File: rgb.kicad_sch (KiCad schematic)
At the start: 0 parts

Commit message: chore: add led matrix
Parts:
- added LED1, LED10, LED11, LED12, LED13, LED14, LED15, LED16, LED17, LED18, LED19, LED2, LED20, LED21, LED22, LED23, LED24, LED25, LED26, LED27, LED28, LED29, LED3, LED30, LED31, LED32, LED33, LED34, LED35, LED36, LED37, LED38, LED39, LED4, LED40, LED41, LED42, LED43, LED44, LED45, LED46, LED5, LED6, LED7, LED8, LED9: MX_SK6812MINI-E, PCM_marbastlib-mx:LED_MX_6028R, symbol PCM_marbastlib-mx:MX_SK6812MINI-E
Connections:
- new net: LED12.2 (DOUT), LED24.3 (DIN)
- new net: LED11.2 (DOUT), LED12.3 (DIN)
- new net: LED26.2 (DOUT), LED27.3 (DIN)
- new net: LED25.2 (DOUT), LED26.3 (DIN)
- new net: LED44.3 (DIN), LED45.2 (DOUT)
- new net: LED45.3 (DIN), LED46.2 (DOUT)
- new net: LED1.2 (DOUT), LED2.3 (DIN)
- new net: LED13.2 (DOUT), LED25.3 (DIN)
- new net: LED42.3 (DIN), LED43.2 (DOUT)
- new net: LED43.3 (DIN), LED44.2 (DOUT)
- new net: LED18.3 (DIN), LED19.2 (DOUT)
- new net: LED19.3 (DIN), LED20.2 (DOUT)
- new net: LED31.2 (DOUT), LED32.3 (DIN)
- new net: LED30.2 (DOUT), LED31.3 (DIN)
- new net: LED13.3 (DIN), LED14.2 (DOUT)
- new net: LED3.2 (DOUT), LED4.3 (DIN)
- new net: LED2.2 (DOUT), LED3.3 (DIN)
- new net: LED16.3 (DIN), LED17.2 (DOUT)
- new net: LED17.3 (DIN), LED18.2 (DOUT)
- new net: LED29.2 (DOUT), LED30.3 (DIN)
- new net: LED28.2 (DOUT), LED29.3 (DIN)
- new net: LED36.2 (DOUT), LED46.3 (DIN)
- new net: LED41.3 (DIN), LED42.2 (DOUT)
- new net: LED5.2 (DOUT), LED6.3 (DIN)
- new net: LED4.2 (DOUT), LED5.3 (DIN)
- new net: LED14.3 (DIN), LED15.2 (DOUT)
- new net: LED15.3 (DIN), LED16.2 (DOUT)
- new net: LED23.3 (DIN), LED24.2 (DOUT)
- new net: LED35.2 (DOUT), LED36.3 (DIN)
- new net: LED22.3 (DIN), LED23.2 (DOUT)
- new net: LED20.3 (DIN), LED21.2 (DOUT)
- new net: LED21.3 (DIN), LED22.2 (DOUT)
- new net: LED33.2 (DOUT), LED34.3 (DIN)
- new net: LED32.2 (DOUT), LED33.3 (DIN)
- new net: LED10.2 (DOUT), LED11.3 (DIN)
- new net: LED6.2 (DOUT), LED7.3 (DIN)
- new net: LED37.3 (DIN), LED38.2 (DOUT)
- new net: LED7.2 (DOUT), LED8.3 (DIN)
- new net: LED8.2 (DOUT), LED9.3 (DIN)
- new net: LED10.3 (DIN), LED9.2 (DOUT)
- new net: LED27.2 (DOUT), LED28.3 (DIN)
- new net: LED34.2 (DOUT), LED35.3 (DIN)
- new net: LED38.3 (DIN), LED39.2 (DOUT)
- new net: LED39.3 (DIN), LED40.2 (DOUT)
- new net: LED40.3 (DIN), LED41.2 (DOUT)
- new net +5V: LED1.1 (VDD), LED10.1 (VDD), LED11.1 (VDD), LED12.1 (VDD), LED13.1 (VDD), LED14.1 (VDD), LED15.1 (VDD), LED16.1 (VDD), LED17.1 (VDD), LED18.1 (VDD), LED19.1 (VDD), LED2.1 (VDD), LED20.1 (VDD), LED21.1 (VDD), LED22.1 (VDD), LED23.1 (VDD), LED24.1 (VDD), LED25.1 (VDD), LED26.1 (VDD), LED27.1 (VDD), LED28.1 (VDD), LED29.1 (VDD), LED3.1 (VDD), LED30.1 (VDD), LED31.1 (VDD), LED32.1 (VDD), LED33.1 (VDD), LED34.1 (VDD), LED35.1 (VDD), LED36.1 (VDD), LED37.1 (VDD), LED38.1 (VDD), LED39.1 (VDD), LED4.1 (VDD), LED40.1 (VDD), LED41.1 (VDD), LED42.1 (VDD), LED43.1 (VDD), LED44.1 (VDD), LED45.1 (VDD), LED46.1 (VDD), LED5.1 (VDD), LED6.1 (VDD), LED7.1 (VDD), LED8.1 (VDD), LED9.1 (VDD)
- new net GND: LED1.4 (VSS), LED10.4 (VSS), LED11.4 (VSS), LED12.4 (VSS), LED13.4 (VSS), LED14.4 (VSS), LED15.4 (VSS), LED16.4 (VSS), LED17.4 (VSS), LED18.4 (VSS), LED19.4 (VSS), LED2.4 (VSS), LED20.4 (VSS), LED21.4 (VSS), LED22.4 (VSS), LED23.4 (VSS), LED24.4 (VSS), LED25.4 (VSS), LED26.4 (VSS), LED27.4 (VSS), LED28.4 (VSS), LED29.4 (VSS), LED3.4 (VSS), LED30.4 (VSS), LED31.4 (VSS), LED32.4 (VSS), LED33.4 (VSS), LED34.4 (VSS), LED35.4 (VSS), LED36.4 (VSS), LED37.4 (VSS), LED38.4 (VSS), LED39.4 (VSS), LED4.4 (VSS), LED40.4 (VSS), LED41.4 (VSS), LED42.4 (VSS), LED43.4 (VSS), LED44.4 (VSS), LED45.4 (VSS), LED46.4 (VSS), LED5.4 (VSS), LED6.4 (VSS), LED7.4 (VSS), LED8.4 (VSS), LED9.4 (VSS)
- new net RGB 5V: LED1.3 (DIN)
- no-connect marks 0 -> 1

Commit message: chore: set up layout
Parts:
- LED1, LED10, LED11, LED12, LED2, LED25, LED26, LED27, LED28, LED29, LED3, LED30, LED31, LED32, LED33, LED34, LED35, LED36, LED4, LED5, LED6, LED7, LED8, LED9: footprint PCM_marbastlib-mx:LED_MX_6028R -> PCM_marbastlib-mx:LED_MX_6028R-ROT
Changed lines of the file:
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@@
 			)
 		)
-		(property "Footprint" "PCM_marbastlib-mx:LED_MX_6028R"
+		(property "Footprint" "PCM_marbastlib-mx:LED_MX_6028R-ROT"
 			(at 330.2 50.8 0)
 			(effects
@@
 			)
 		)
-		(property "Footprint" "PCM_marbastlib-mx:LED_MX_6028R"
+		(property "Footprint" "PCM_marbastlib-mx:LED_MX_6028R-ROT"
 			(at 76.2 127 0)
 			(effects
@@
 			)
 		)
-		(property "Footprint" "PCM_marbastlib-mx:LED_MX_6028R"
+		(property "Footprint" "PCM_marbastlib-mx:LED_MX_6028R-ROT"
 			(at 50.8 50.8 0)
 			(effects
@@
 			)
 		)
-		(property "Footprint" "PCM_marbastlib-mx:LED_MX_6028R"
+		(property "Footprint" "PCM_marbastlib-mx:LED_MX_6028R-ROT"
 			(at 50.8 127 0)
 			(effects
@@
 			)
 		)
-		(property "Footprint" "PCM_marbastlib-mx:LED_MX_6028R"
+		(property "Footprint" "PCM_marbastlib-mx:LED_MX_6028R-ROT"
 			(at 203.2 127 0)
 			(effects
@@
 			)
 		)
-		(property "Footprint" "PCM_marbastlib-mx:LED_MX_6028R"
+		(property "Footprint" "PCM_marbastlib-mx:LED_MX_6028R-ROT"
 			(at 101.6 50.8 0)
 			(effects
@@
 			)
 		)
-		(property "Footprint" "PCM_marbastlib-mx:LED_MX_6028R"
+		(property "Footprint" "PCM_marbastlib-mx:LED_MX_6028R-ROT"
 			(at 152.4 127 0)
 			(effects
@@
 			)
 		)
-		(property "Footprint" "PCM_marbastlib-mx:LED_MX_6028R"
+		(property "Footprint" "PCM_marbastlib-mx:LED_MX_6028R-ROT"
 			(at 152.4 50.8 0)
 			(effects
@@
 			)
 		)
-		(property "Footprint" "PCM_marbastlib-mx:LED_MX_6028R"
+		(property "Footprint" "PCM_marbastlib-mx:LED_MX_6028R-ROT"
 			(at 330.2 127 0)
 			(effects
@@
 			)
 		)
-		(property "Footprint" "PCM_marbastlib-mx:LED_MX_6028R"
+		(property "Footprint" "PCM_marbastlib-mx:LED_MX_6028R-ROT"
 			(at 127 50.8 0)
 			(effects
@@
 			)
 		)
-		(property "Footprint" "PCM_marbastlib-mx:LED_MX_6028R"
+		(property "Footprint" "PCM_marbastlib-mx:LED_MX_6028R-ROT"
 			(at 254 127 0)
 			(effects
@@
 			)
 		)
-		(property "Footprint" "PCM_marbastlib-mx:LED_MX_6028R"
+		(property "Footprint" "PCM_marbastlib-mx:LED_MX_6028R-ROT"
 			(at 304.8 50.8 0)
 			(effects
@@
 			)
 		)
-		(property "Footprint" "PCM_marbastlib-mx:LED_MX_6028R"
+		(property "Footprint" "PCM_marbastlib-mx:LED_MX_6028R-ROT"
 			(at 177.8 50.8 0)
 			(effects
@@
 			)
 		)
-		(property "Footprint" "PCM_marbastlib-mx:LED_MX_6028R"
+		(property "Footprint" "PCM_marbastlib-mx:LED_MX_6028R-ROT"
 			(at 203.2 50.8 0)
 			(effects
@@
 			)
 		)
-		(property "Footprint" "PCM_marbastlib-mx:LED_MX_6028R"
+		(property "Footprint" "PCM_marbastlib-mx:LED_MX_6028R-ROT"
 			(at 228.6 50.8 0)
 			(effects
@@
 			)
 		)
-		(property "Footprint" "PCM_marbastlib-mx:LED_MX_6028R"
+		(property "Footprint" "PCM_marbastlib-mx:LED_MX_6028R-ROT"
 			(at 279.4 50.8 0)
 			(effects
@@
 			)
 		)
-		(property "Footprint" "PCM_marbastlib-mx:LED_MX_6028R"
+		(property "Footprint" "PCM_marbastlib-mx:LED_MX_6028R-ROT"
 			(at 76.2 50.8 0)
 			(effects
@@
 			)
 		)
-		(property "Footprint" "PCM_marbastlib-mx:LED_MX_6028R"
+		(property "Footprint" "PCM_marbastlib-mx:LED_MX_6028R-ROT"
 			(at 127 127 0)
 			(effects
@@
 			)
 		)
-		(property "Footprint" "PCM_marbastlib-mx:LED_MX_6028R"
+		(property "Footprint" "PCM_marbastlib-mx:LED_MX_6028R-ROT"
 			(at 279.4 127 0)
 			(effects
@@
 			)
 		)
-		(property "Footprint" "PCM_marbastlib-mx:LED_MX_6028R"
+		(property "Footprint" "PCM_marbastlib-mx:LED_MX_6028R-ROT"
 			(at 254 50.8 0)
 			(effects
@@
 			)
 		)
-		(property "Footprint" "PCM_marbastlib-mx:LED_MX_6028R"
+		(property "Footprint" "PCM_marbastlib-mx:LED_MX_6028R-ROT"
 			(at 101.6 127 0)
 			(effects
@@
 			)
 		)
-		(property "Footprint" "PCM_marbastlib-mx:LED_MX_6028R"
+		(property "Footprint" "PCM_marbastlib-mx:LED_MX_6028R-ROT"
 			(at 304.8 127 0)
 			(effects
@@
 			)
 		)
-		(property "Footprint" "PCM_marbastlib-mx:LED_MX_6028R"
+		(property "Footprint" "PCM_marbastlib-mx:LED_MX_6028R-ROT"
 			(at 177.8 127 0)
 			(effects
@@
 			)
 		)
-		(property "Footprint" "PCM_marbastlib-mx:LED_MX_6028R"
+		(property "Footprint" "PCM_marbastlib-mx:LED_MX_6028R-ROT"
 			(at 228.6 127 0)
 			(effects

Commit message: chore: open-drain for rgb
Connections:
- net RGB 5V renamed RGB5V
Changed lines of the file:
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@@
 		)
 	)
-	(global_label "RGB 5V"
+	(global_label "RGB5V"
 		(shape input)
 		(at 43.18 50.8 180)
@@
 		)
 		(property "Intersheetrefs" "${INTERSHEET_REFS}"
-			(at 33.1191 50.8 0)
+			(at 34.0867 50.8 0)
 			(effects
 				(font

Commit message: chore: add mounting holes
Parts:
- LED1: LCSC (none) -> C5149201
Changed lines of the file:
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@@
+			)
+		)
+		(property "LCSC" "C5149201"
+			(at 50.8 50.8 0)
+			(effects
+				(font
+					(size 1.27 1.27)
+				)
+				(hide yes)
 			)
 		)

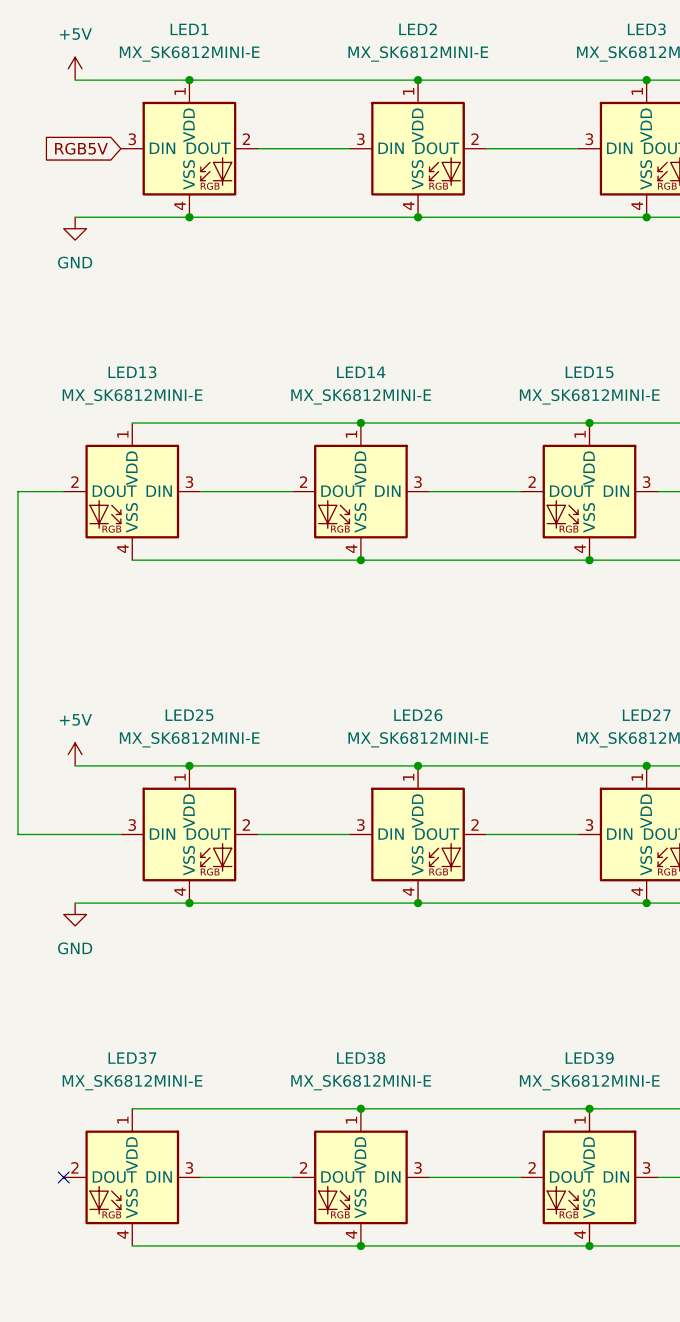
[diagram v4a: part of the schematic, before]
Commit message: chore: add decoupling caps for 5v led lines
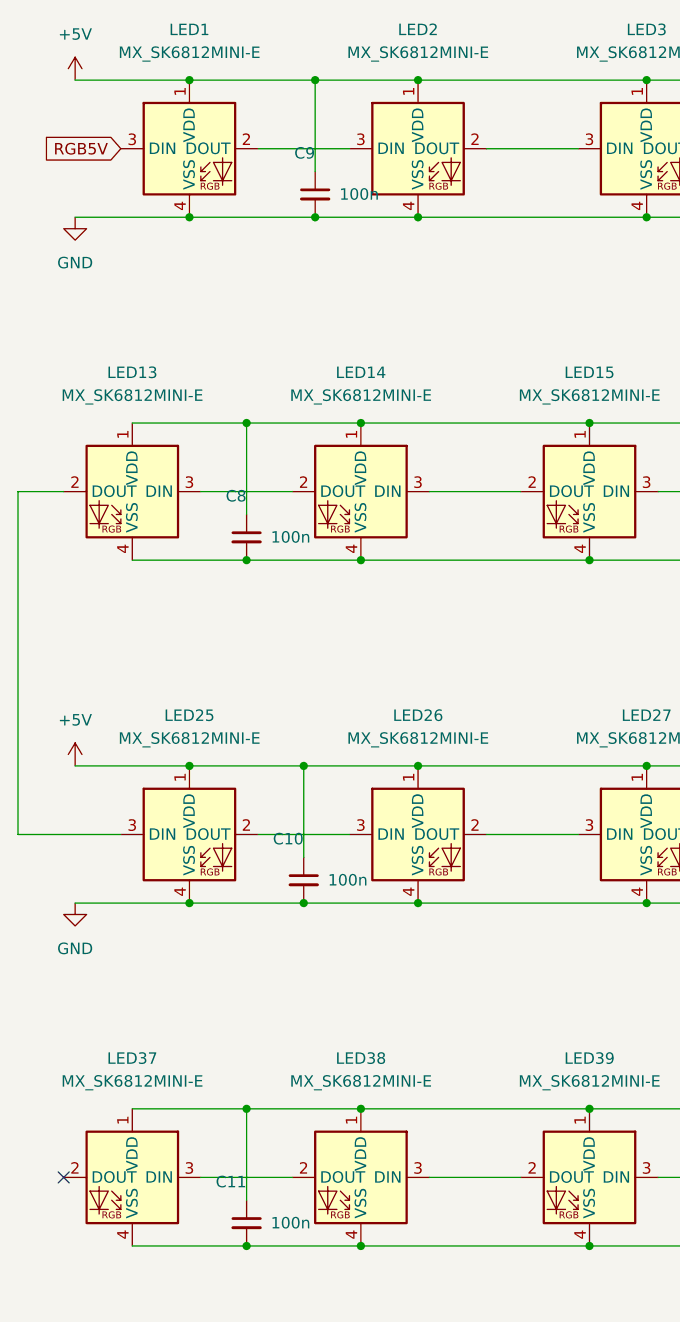
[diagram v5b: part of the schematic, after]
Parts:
- added C10, C11, C8, C9: 100n, Capacitor_SMD:C_0402_1005Metric, symbol Device:C_Small
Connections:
- net +5V: now also C10.1, C11.1, C8.1, C9.1
- net GND: now also C10.2, C11.2, C8.2, C9.2

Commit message: chore: updated rbb schema
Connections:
- net RGB5V: now also LED46.3 (DIN); no longer LED1.3 (DIN)
- net at LED12.2 (DOUT): no longer LED24.3 (DIN)
- net at LED13.2 (DOUT): now also LED1.3 (DIN); no longer LED25.3 (DIN)
- net at LED36.2 (DOUT): now also LED24.3 (DIN); no longer LED46.3 (DIN)
- net at LED37.2 (DOUT): now also LED25.3 (DIN)
